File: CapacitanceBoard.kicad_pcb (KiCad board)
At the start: 2 copper layers, 17.7 x 24.2 mm, 15 parts

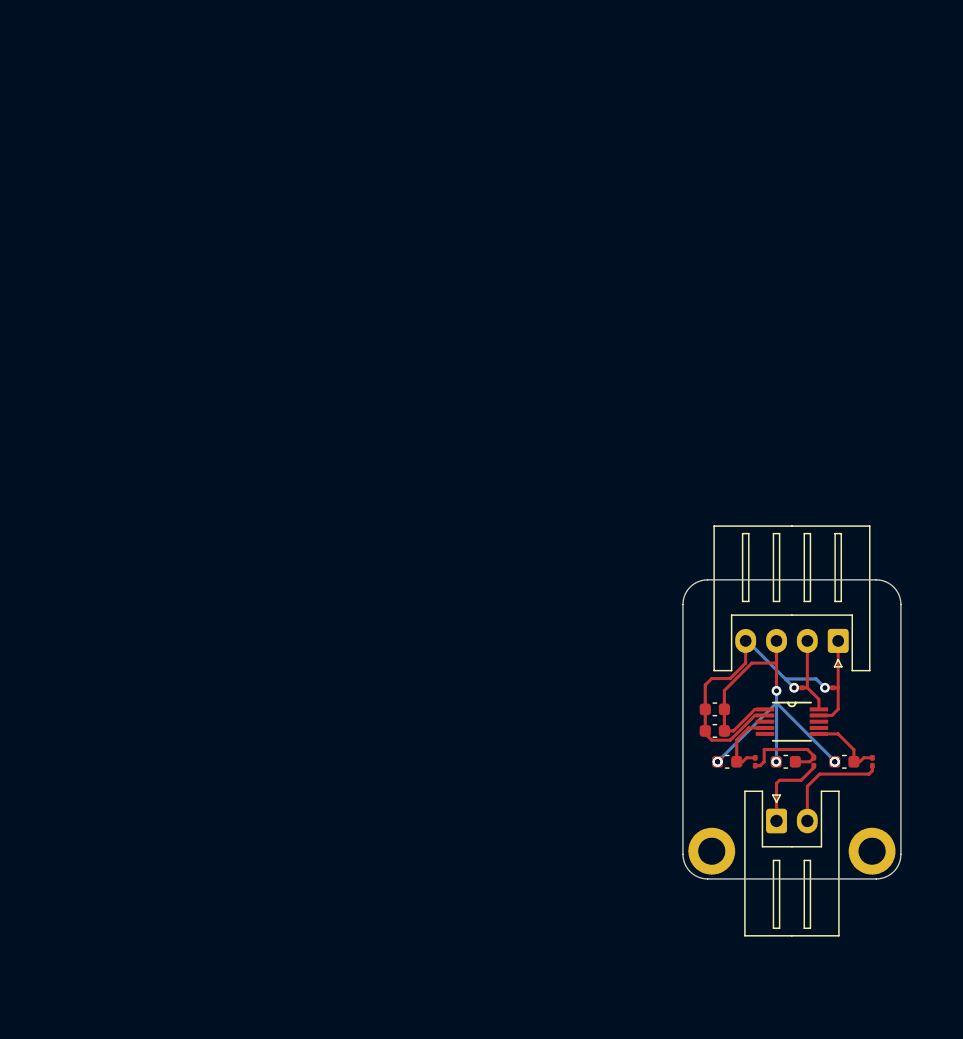
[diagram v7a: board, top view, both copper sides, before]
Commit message: Improved schematic and updated PCB references and layout.
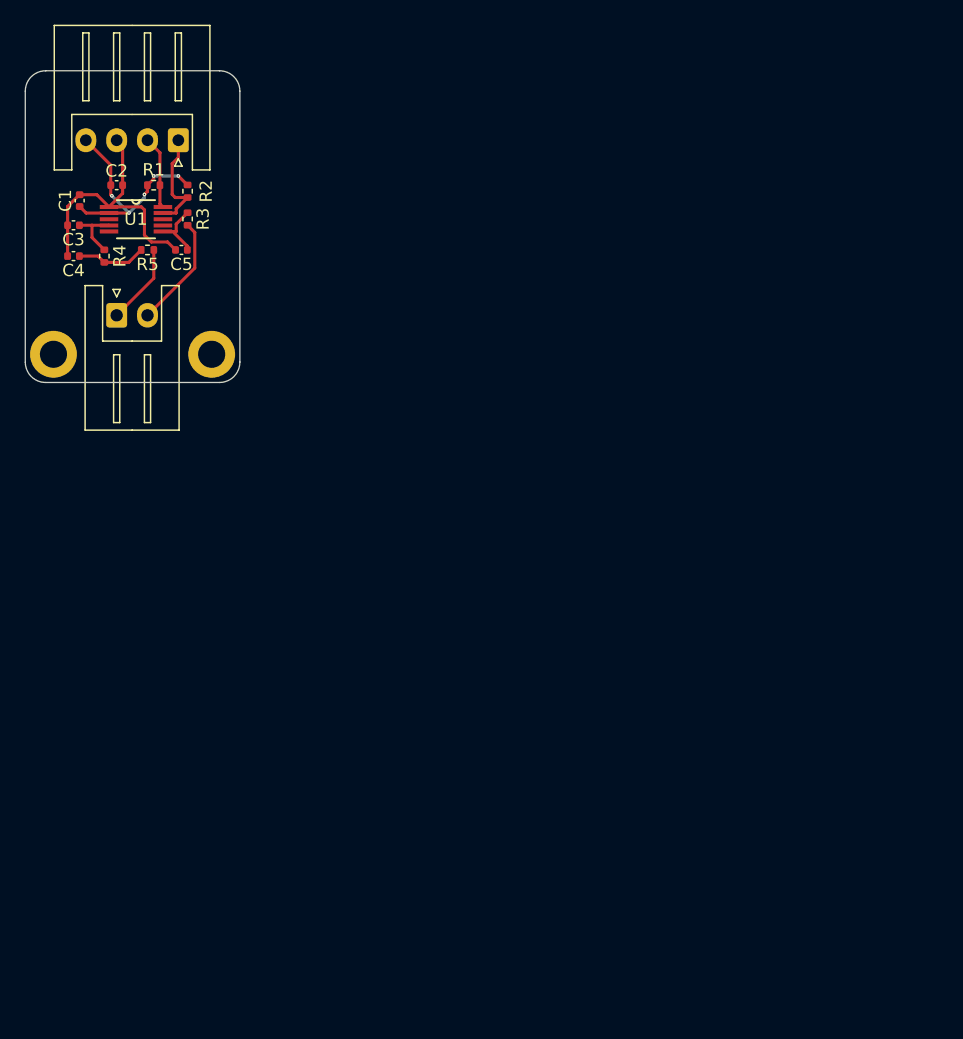
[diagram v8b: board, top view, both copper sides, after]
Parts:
- removed the REF** at (179.0, 122.5)
- removed the REF** at (176.0, 125.8)
- removed the REF** at (179.5, 119.8)
- removed the REF** at (177.8, 130.6)
- removed the REF** at (172.8, 123.2)
- removed the REF** at (183.2, 125.8)
- removed the REF** at (185.5, 125.8)
- removed the REF** at (182.0, 119.8)
- removed the REF** at (182.8, 116.0)
- removed the REF** at (180.8, 125.8)
- removed the REF** at (172.8, 121.5)
- removed the REF** at (173.8, 125.8)
- removed the REF** at (185.5, 133.0)
- removed the REF** at (178.5, 125.8)
- removed the REF** at (172.5, 133.0)
- added ?: , , F.Cu at (119.1, 92.7)
- added C1: 0.1u, Capacitor_SMD:C_0402_1005Metric, F.Cu at (121.2, 80.2)
- added C2: 10u, Capacitor_SMD:C_0402_1005Metric, F.Cu at (124.2, 79.0)
- added C3: 22p, Capacitor_SMD:C_0402_1005Metric, F.Cu at (120.8, 82.2)
- added C4: 68p, Capacitor_SMD:C_0402_1005Metric, F.Cu at (120.8, 84.8)
- added C5: 47p, Capacitor_SMD:C_0402_1005Metric, F.Cu at (129.5, 84.2)
- added J1: Conn_01x04_Pin, Connector_JST:JST_XH_S4B-XH-A_1x04_P2.50mm_Horizontal, F.Cu at (129.2, 75.4)
- added J2: Conn_01x02_Pin, Connector_JST:JST_XH_S2B-XH-A_1x02_P2.50mm_Horizontal, F.Cu at (124.2, 89.5)
- added R1: 1k, Resistor_SMD:R_0402_1005Metric, F.Cu at (127.2, 79.0)
- added R2: 1k, Resistor_SMD:R_0402_1005Metric, F.Cu at (130.0, 79.5)
- added R3: 10k, Resistor_SMD:R_0402_1005Metric, F.Cu at (130.0, 81.7)
- added R4: 82k, Resistor_SMD:R_0402_1005Metric, F.Cu at (123.2, 84.8)
- added R5: 39k, Resistor_SMD:R_0402_1005Metric, F.Cu at (126.8, 84.2)
- added REF**: MountingHole_2.2mm_M2_DIN965_Pad, MountingHole:MountingHole_2.2mm_M2_DIN965_Pad, F.Cu at (132.0, 92.7)
- added U1: AD7150BRMZ, AD7150BRMZ:SOP50P490X110-10N, F.Cu at (125.8, 81.8)
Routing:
- net (no net): track 114.0 -> 0.00 mm, vias 8 -> 0
- net Earth: track 0.00 -> 22.3 mm
- net VDD: track 0.00 -> 18.4 mm, vias 0 -> 5
- net Net-(J2-Pin_2): track 0.00 -> 9.13 mm
- net /SCL: track 0.00 -> 8.67 mm
- net Net-(J2-Pin_1): track 0.00 -> 6.55 mm
- net /SDA: track 0.00 -> 5.92 mm
- net Net-(C4-Pad1): track 0.00 -> 5.64 mm
- net /CIN1: track 0.00 -> 4.81 mm
- net /EXC1: track 0.00 -> 4.17 mm
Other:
- board size 17.7 x 24.2 mm -> 17.4 x 25.3 mm
- board text added: "Capacitive Fill Sensor"
- board text added: "U1"
- board text removed: "Capacitive Fill Board"
